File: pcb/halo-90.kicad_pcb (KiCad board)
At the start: 4 copper layers, 24 x 24 mm, 103 parts, among them J1 TC2030-SWIM-NL, U1 STM8151G6U6, U2 SC7A20HTR, U3 HAL2041SO

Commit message: Added CS trace and updated battery.
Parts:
- BT1: value CR-2032 -> BAT-HLD-001
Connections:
- U2 pad 10: unconnected-(U2-CS-Pad10) -> +3V
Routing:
- net +3V: track 108.0 -> 109.3 mm

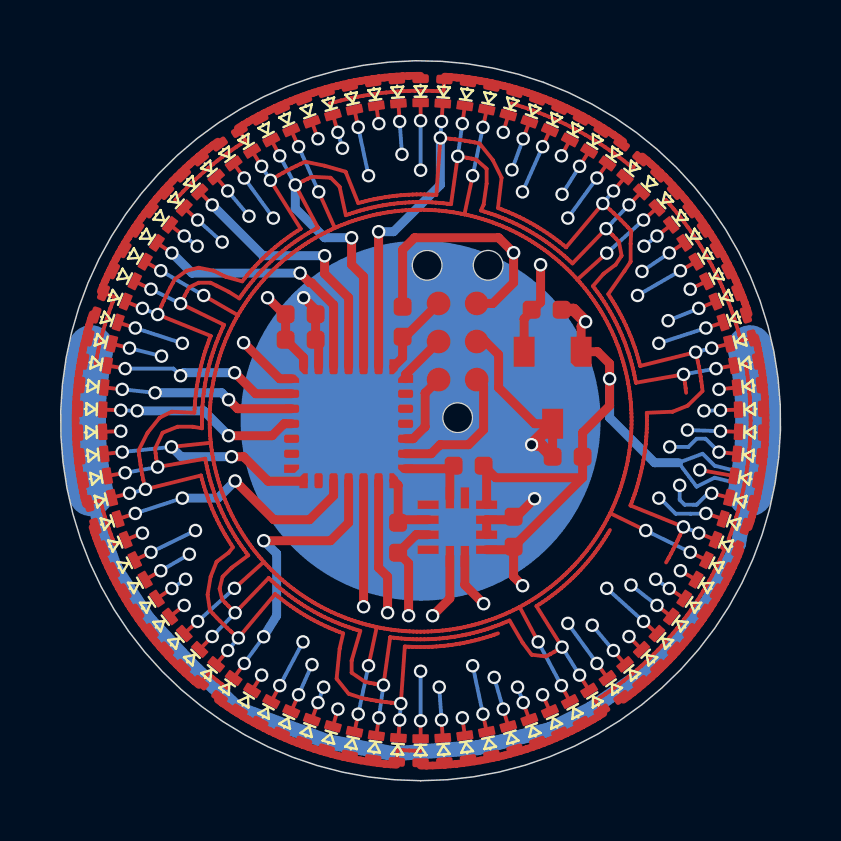
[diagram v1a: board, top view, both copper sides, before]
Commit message: Added mic and rerouted
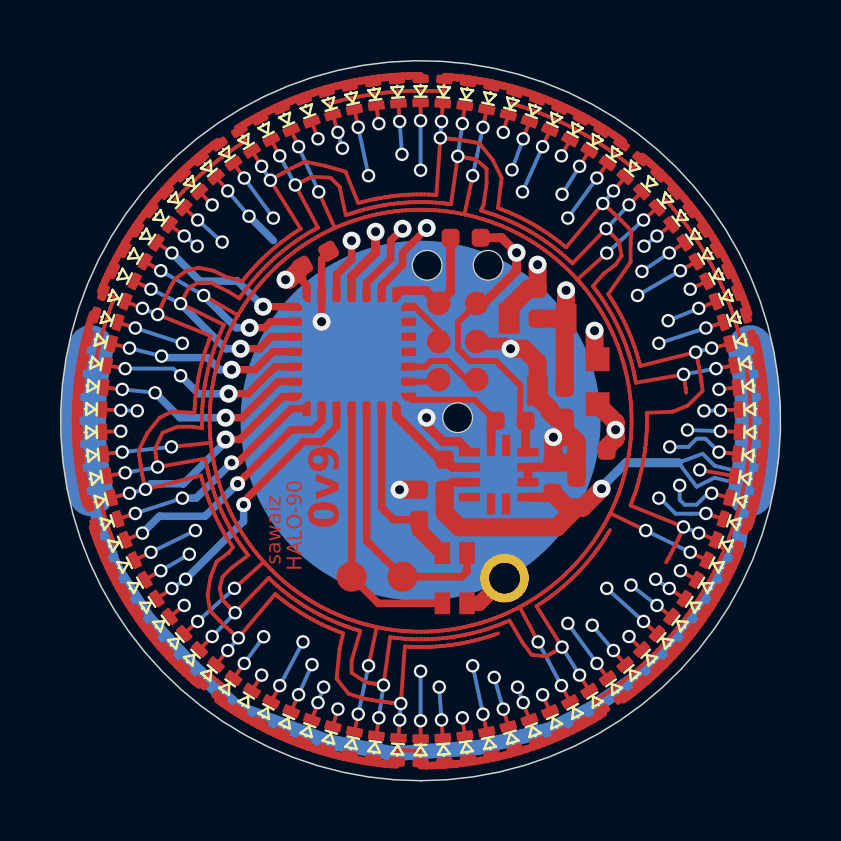
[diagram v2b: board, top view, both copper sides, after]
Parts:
- added C5: 100nF, C-0402:C-0402, F.Cu at (-0.05, 2.80)
- added Q1: ALS-PT19, ALS-PT19:ALS-PT19, F.Cu at (5.90, -1.30)
- added Q2: SPH0641LU4H, SPH0641LU4H:SPH0641LU4H, F.Cu at (2.80, 5.25)
- added R5: 10k, R-0402:R-0402, F.Cu at (5.70, 1.00)
- added TP1: TestPoint_D1.0, tooling:TestPoint_Pad_D1.0mm, F.Cu at (-2.30, 5.20)
- added TP2: TestPoint_D1.0, tooling:TestPoint_Pad_D1.0mm, F.Cu at (-0.60, 5.20)
- moved C4 11.0 mm to (5.20, 2.40), turned to 90 degrees
- moved R3 3.50 mm to (1.50, -6.10), turned to 180 degrees
- moved C2 2.75 mm to (-3.50, -5.40), turned to 30 degrees
- moved R1 2.61 mm to (0.80, 1.80)
- moved U1 2.40 mm to (-2.30, -2.30)
- moved U2 2.23 mm to (2.60, 1.80)
- moved C1 2.22 mm to (4.40, 1.90)
- moved R2 2.05 mm to (3.00, 0.00)
- moved C3 1.80 mm to (4.80, -0.60), turned to -90 degrees
- moved U3 1.21 mm to (3.90, -2.20)
- moved R4 0.36 mm to (3.90, -3.90), turned to -90 degrees
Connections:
- C3 pad 1: +3V -> HALL_{PWR}
- J1 pad 1: RX -> TX
- J1 pad 2: TX -> RX
- R4 pad 2: +3V -> HALL_{PWR}
- U1 pad 10: CPX-5 -> CPX-1
- U1 pad 11: CPX-4 -> CPX-8
- U1 pad 12: unconnected-(U1-PB0-Pad12) -> CPX-6
- U1 pad 13: unconnected-(U1-PB1-Pad13) -> CPX-5
- U1 pad 14: unconnected-(U1-PB2-Pad14) -> CPX-0
- U1 pad 15: CPX-2 -> CPX-9
- U1 pad 16: unconnected-(U1-PB4-Pad16) -> CPX-7
- U1 pad 17: CPX-9 -> CPX-4
- U1 pad 18: CPX-8 -> PDM_DTA
- U1 pad 19: XL-INT2 -> PDM_CLK
- U1 pad 2: CPX-0 -> HALL
- U1 pad 20: XL-INT1 -> PWR_{MIC}
- U1 pad 3: CPX-1 -> HALL_{PWR}
- U1 pad 4: CPX-7 -> ALR_{PWR}
- U1 pad 5: CPX-3 -> ALR
- U1 pad 8: HALL -> CPX-3
- U1 pad 9: CPX-6 -> CPX-2
- U2 pad 1: unconnected-(U2-SDO-Pad1) -> GND
- U3 pad 1: +3V -> HALL_{PWR}
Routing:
- net GND: track 12.2 -> 34.0 mm, vias 3 -> 5
- net ALR: track 0.00 -> 16.9 mm, vias 0 -> 2
- net HALL_{PWR}: track 0.00 -> 14.6 mm, vias 0 -> 2
- net ALR_{PWR}: track 0.00 -> 13.3 mm, vias 0 -> 2
- net XL-INT2: track 10.7 -> 0.00 mm, vias 2 -> 0
- net PDM_DTA: track 0.00 -> 8.99 mm
- net PDM_CLK: track 0.00 -> 8.93 mm
- net XL-INT1: track 8.81 -> 0.00 mm, vias 2 -> 0
- net +3V: track 109.3 -> 100.7 mm, vias 6 -> 3
- net PWR_{MIC}: track 0.00 -> 6.15 mm
- net HALL: track 16.2 -> 11.1 mm
- net RX: track 4.70 -> 1.03 mm
- net CPX-3: track 102.8 -> 99.5 mm
- net CPX-1: track 103.3 -> 100.4 mm
- net CPX-0: track 105.5 -> 103.0 mm
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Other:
- board text added: "0v9"
- board text added: "HALO-90"
- board text added: "KOLIBRI"
- board text added: "sawaiz"
- board text removed: "KOLIBRI sawaiz 2026-03 HALO-90 0v8"

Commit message: 0v9 with ALR, XL, Mic added order placed
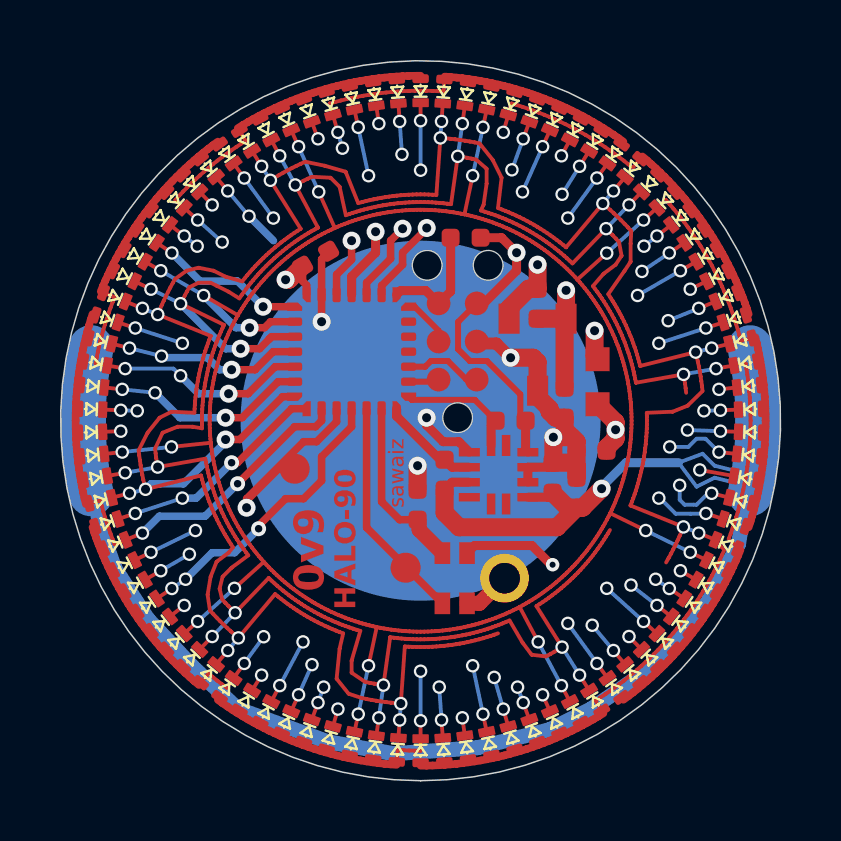
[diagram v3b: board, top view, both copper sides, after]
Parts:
- moved TP2 5.09 mm to (-4.20, 1.60)
- moved TP1 1.82 mm to (-0.50, 4.90)
- moved C5 0.05 mm to (-0.10, 2.80)
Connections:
- U1 pad 17: CPX-4 -> PDM_CLK
- U1 pad 18: PDM_DTA -> CPX-4
- U1 pad 19: PDM_CLK -> PDM_DTA
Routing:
- net PDM_CLK: track 8.93 -> 21.3 mm, vias 0 -> 2
- net GND: track 34.0 -> 36.1 mm
- net PDM_DTA: track 8.99 -> 7.53 mm
- net CPX-4: track 101.1 -> 101.8 mm
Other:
- board text added: "KOLIBRI 2026-06"
- board text removed: "KOLIBRI"
